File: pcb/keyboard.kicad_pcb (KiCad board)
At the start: 4 copper layers, 304.8 x 119.1 mm, 197 parts, among them J1 Conn_ARM_JTAG_SWD_10, J2 USB_C_Receptacle_USB2.0_16P, J3 Conn_Coaxial, K1 KEYSW, K10 KEYSW, K11 KEYSW, K12 KEYSW, K13 KEYSW, K14 KEYSW, K15 KEYSW, K16 KEYSW, K17 KEYSW, K18 KEYSW, K19 KEYSW, K2 KEYSW, K20 KEYSW, K21 KEYSW, K22 KEYSW, K23 KEYSW, K24 KEYSW, K25 KEYSW, K26 KEYSW, K27 KEYSW, K28 KEYSW, K29 KEYSW, K3 KEYSW, K30 KEYSW, K31 KEYSW, K32 KEYSW, K33 KEYSW, K34 KEYSW, K35 KEYSW, K36 KEYSW, K37 KEYSW, K38 KEYSW, K39 KEYSW, K4 KEYSW, K40 KEYSW, K41 KEYSW, K42 KEYSW, K43 KEYSW, K45 KEYSW, K46 KEYSW, K47 KEYSW, K48 KEYSW, K49 KEYSW, K5 KEYSW, K50 KEYSW, K51 KEYSW, K52 KEYSW, K53 KEYSW, K54 KEYSW, K55 KEYSW, K56 KEYSW, K57 KEYSW, K58 KEYSW, K59 KEYSW, K6 KEYSW, K60 KEYSW, K61 KEYSW, K62 KEYSW, K63 KEYSW, K67 KEYSW, K7 KEYSW, K70 KEYSW, K71 KEYSW, K72 KEYSW, K73 KEYSW, K74 KEYSW, K75 KEYSW, K8 KEYSW, K9 KEYSW, Q1 FDN340P, Q2 FS8025A, Q3 FDN340P, SW1 SW_SPST, SW2 SW_SPST, U1 nRF52840, U2 TP4056-42-ESOP8, U3 DW01A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

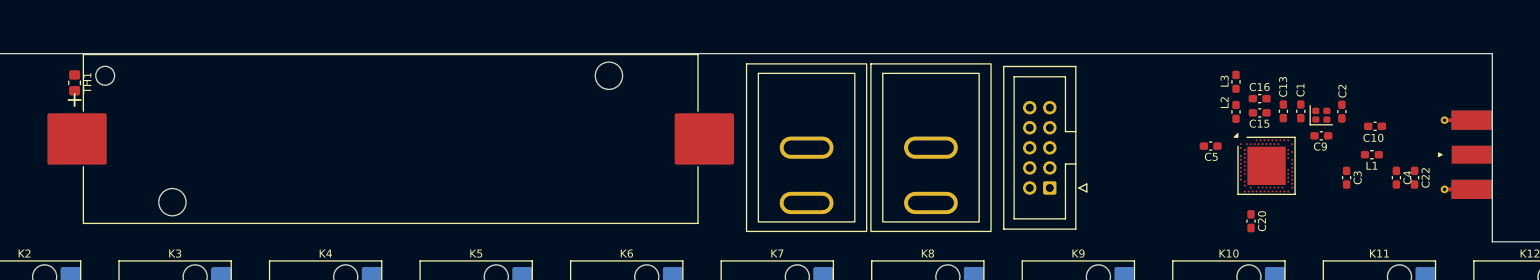
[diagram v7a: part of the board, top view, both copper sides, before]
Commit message: Fixed switch footprint
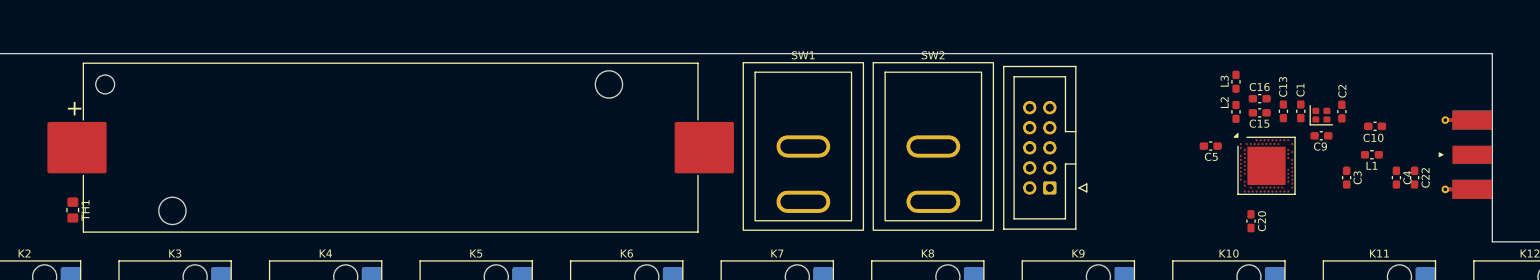
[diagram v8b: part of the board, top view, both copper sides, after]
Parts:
- moved TH1 16.1 mm to (82.3, 96.0)
- moved BT1 1.10 mm to (122.5, 88.1)
- moved SW1 0.44 mm to (174.8, 88.0)
- moved SW2 0.34 mm to (191.2, 88.0)
- moved J3 0.10 mm to (257.7, 89.0)
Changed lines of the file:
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@@
 		)
 	)
+	(footprint "My_Footprints:Legion SS11"
+		(layer "F.Cu")
+		(at 191.2 87.95)
+		(property "Reference" "SW2"
+			(at 0 -11.5 0)
+			(unlocked yes)
+			(layer "F.SilkS")
+			(effects
+				(font
+					(size 1 1)
+					(thickness 0.1)
+				)
+			)
+		)
+		(property "Value" "SW_SPST"
+			(at 0 11.8 0)
+			(unlocked yes)
+			(layer "F.Fab")
+			(effects
+				(font
+					(size 1 1)
+					(thickness 0.15)
+				)
+			)
+		)
+		(property "Datasheet" ""
+			(at 0 0 0)
+			(unlocked yes)
+			(layer "F.Fab")
+			(hide yes)
+			(effects
+				(font
+					(size 1 1)
+					(thickness 0.15)
+				)
+			)
+		)
+		(property "Description" "Single Pole Single Throw (SPST) switch"
+			(at 0 0 0)
+			(unlocked yes)
+			(layer "F.Fab")
+			(hide yes)
+			(effects
+				(font
+					(size 1 1)
+					(thickness 0.15)
+				)
+			)
+		)
+		(sheetname "/power/")
+		(sheetfile "usb.kicad_sch")
+		(units
+			(unit
+				(name "A")
+				(pins "1" "2")
+			)
+		)
+		(attr smd)
+		(duplicate_pad_numbers_are_jumpers no)
+		(fp_rect
+			(start -7.6 -10.6)
+			(end 7.6 10.6)
+			(stroke
+				(width 0.1)
+				(type default)
+			)
+			(fill no)
+			(layer "F.SilkS")
+		)
+		(fp_rect
+			(start -6.101237 -9.400531)
+			(end 6.098763 9.399469)
+			(stroke
+				(width 0.1)
+				(type default)
+			)
+			(fill no)
+			(layer "F.SilkS")
+		)
+		(fp_text user "${REFERENCE}"
+			(at 0 -2.45 0)
+			(unlocked yes)
+			(layer "F.Fab")
+			(effects
+				(font
+					(size 1 1)
+					(thickness 0.15)
+				)
+			)
+		)
+		(pad "1" thru_hole roundrect
+			(at 0 7)
+			(size 6.82 2.82)
+			(drill oval 5.82 1.82)
+			(layers "*.Cu" "*.Mask")
+			(remove_unused_layers no)
+			(roundrect_rratio 0.5)
+			(net "Net-(D64-K)")
+			(pinfunction "A_1")
+			(pintype "passive")
+		)
+		(pad "2" thru_hole roundrect
+			(at 0 0)
+			(size 6.82 2.82)
+			(drill oval 5.82 1.82)
+			(layers "*.Cu" "*.Mask")
+			(remove_unused_layers no)
+			(roundrect_rratio 0.5)
+			(net "/power/BAT_POS")
+			(pinfunction "B_2")
+			(pintype "passive")
+		)
+		(embedded_fonts no)
+	)
 	(footprint "Resistor_SMD:R_0805_2012Metric_Pad1.20x1.40mm_HandSolder"
 		(layer "F.Cu")
@@
 	(footprint "Resistor_SMD:R_0805_2012Metric_Pad1.20x1.40mm_HandSolder"
 		(layer "F.Cu")
-		(at 82.53 79.9 -90)
+		(at 82.3 96 -90)
 		(descr "Resistor SMD 0805 (2012 Metric), square (rectangular) end terminal, IPC-7351 nominal with elongated pad for handsoldering. (Body size source: IPC-SM-782 page 72, https://www.pcb-3d.com/wordpress/wp-content/uploads/ipc-sm-782a_amendment_1_and_2.pdf)")
 		(tags "resistor handsolder")
@@
 		)
 		(fp_text user "${REFERENCE}"
-			(at 0 0 90)
+			(at 0.1 0 90)
 			(layer "F.Fab")
 			(effects
@@
 	(footprint "My_Footprints:Legion SS11"
 		(layer "F.Cu")
-		(at 175.1625 88.1)
+		(at 174.75 87.95)
 		(property "Reference" "SW1"
 			(at 0 -11.5 0)
 			(unlocked yes)
 			(layer "F.SilkS")
-			(hide yes)
 			(effects
 				(font
@@
 			(unlocked yes)
 			(layer "F.Fab")
-			(hide yes)
 			(effects
 				(font
@@
 		)
 		(fp_text user "${REFERENCE}"
-			(at 0 -2.65 0)
+			(at 0 -2.45 0)
 			(unlocked yes)
 			(layer "F.Fab")
@@
 			(drill oval 5.82 1.82)
 			(layers "*.Cu" "*.Mask")
-			(remove_unused_layers yes)
-			(keep_end_layers yes)
-			(zone_layer_connections)
+			(remove_unused_layers no)
 			(roundrect_rratio 0.5)
 			(net "GND")
@@
 			(drill oval 5.82 1.82)
 			(layers "*.Cu" "*.Mask")
-			(remove_unused_layers yes)
-			(keep_end_layers yes)
-			(zone_layer_connections)
+			(remove_unused_layers no)
 			(roundrect_rratio 0.5)
 			(net "/~{RESET}")
@@
 	(footprint "Connector_Coaxial:SMA_Molex_73251-1153_EdgeMount_Horizontal"
 		(layer "F.Cu")
-		(at 257.61 89 180)
+		(at 257.71 89 180)
 		(descr "Molex SMA RF Connectors, Edge Mount, https://tools.molex.com/pdm_docs/sd/732511150_sd.pdf")
 		(tags "sma edge")
@@
 		)
 	)
-	(footprint "My_Footprints:Legion SS11"
-		(layer "F.Cu")
-		(at 190.9 88.1)
-		(property "Reference" "SW2"
-			(at 0 -11.5 0)
-			(unlocked yes)
-			(layer "F.SilkS")
-			(hide yes)
-			(effects
-				(font
-					(size 1 1)
-					(thickness 0.1)
-				)
-			)
-		)
-		(property "Value" "SW_SPST"
-			(at 0 11.8 0)
-			(unlocked yes)
-			(layer "F.Fab")
-			(hide yes)
-			(effects
-				(font
-					(size 1 1)
-					(thickness 0.15)
-				)
-			)
-		)
-		(property "Datasheet" ""
-			(at 0 0 0)
-			(unlocked yes)
-			(layer "F.Fab")
-			(hide yes)
-			(effects
-				(font
-					(size 1 1)
-					(thickness 0.15)
-				)
-			)
-		)
-		(property "Description" "Single Pole Single Throw (SPST) switch"
-			(at 0 0 0)
-			(unlocked yes)
-			(layer "F.Fab")
-			(hide yes)
-			(effects
-				(font
-					(size 1 1)
-					(thickness 0.15)
-				)
-			)
-		)
-		(sheetname "/power/")
-		(sheetfile "usb.kicad_sch")
-		(units
-			(unit
-				(name "A")
-				(pins "1" "2")
-			)
-		)
-		(attr smd)
-		(duplicate_pad_numbers_are_jumpers no)
-		(fp_rect
-			(start -7.6 -10.6)
-			(end 7.6 10.6)
-			(stroke
-				(width 0.1)
-				(type default)
-			)
-			(fill no)
-			(layer "F.SilkS")
-		)
-		(fp_rect
-			(start -6.101237 -9.400531)
-			(end 6.098763 9.399469)
-			(stroke
-				(width 0.1)
-				(type default)
-			)
-			(fill no)
-			(layer "F.SilkS")
-		)
-		(fp_text user "${REFERENCE}"
-			(at 0 -2.45 0)
-			(unlocked yes)
-			(layer "F.Fab")
-			(effects
-				(font
-					(size 1 1)
-					(thickness 0.15)
-				)
-			)
-		)
-		(pad "1" thru_hole roundrect
-			(at 0 7)
-			(size 6.82 2.82)
-			(drill oval 5.82 1.82)
-			(layers "*.Cu" "*.Mask")
-			(remove_unused_layers yes)
-			(keep_end_layers yes)
-			(zone_layer_connections)
-			(roundrect_rratio 0.5)
-			(net "Net-(D64-K)")
-			(pinfunction "A_1")
-			(pintype "passive")
-		)
-		(pad "2" thru_hole roundrect
-			(at 0 0)
-			(size 6.82 2.82)
-			(drill oval 5.82 1.82)
-			(layers "*.Cu" "*.Mask")
-			(remove_unused_layers yes)
-			(keep_end_layers yes)
-			(zone_layer_connections)
-			(roundrect_rratio 0.5)
-			(net "/power/BAT_POS")
-			(pinfunction "B_2")
-			(pintype "passive")
-		)
-		(embedded_fonts no)
-	)
 	(footprint "Fuse:Fuse_0402_1005Metric_Pad0.77x0.64mm_HandSolder"
 		(layer "F.Cu")
@@
 	(footprint "Battery:BatteryHolder_Keystone_1042_1x18650"
 		(layer "F.Cu")
-		(at 122.53 87)
+		(at 122.53 88.1)
 		(descr "Battery holder, Keystone 1042, battery type 1x18650, http://www.keyelco.com/product.cfm/product_id/918")
 		(tags "horizontal single")
